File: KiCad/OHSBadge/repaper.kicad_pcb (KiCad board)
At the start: 2 copper layers, 101.6 x 78.7 mm, 76 parts, among them J4 ZIF-40-0.5, P1 PCB, P2 ISP, P3 FTDI, P4 C3SB, P6 3V3_SEL, Q1 AP2305, Q2 2N7002KW, Q3 BSS84W, Q4 2N7002KW, Q5 2N7002KW, Q6 2N7002KW, Q7 BSS84W, SW1 UP, SW2 SEL, SW3 DOWN, SW4 RST, U1 MCP9700AT-E/TT, U2 ATMEGA328-AU-ND, U3 MCP1700T-33, U4 TXS0108, X1 CRYSTAL_8MHz

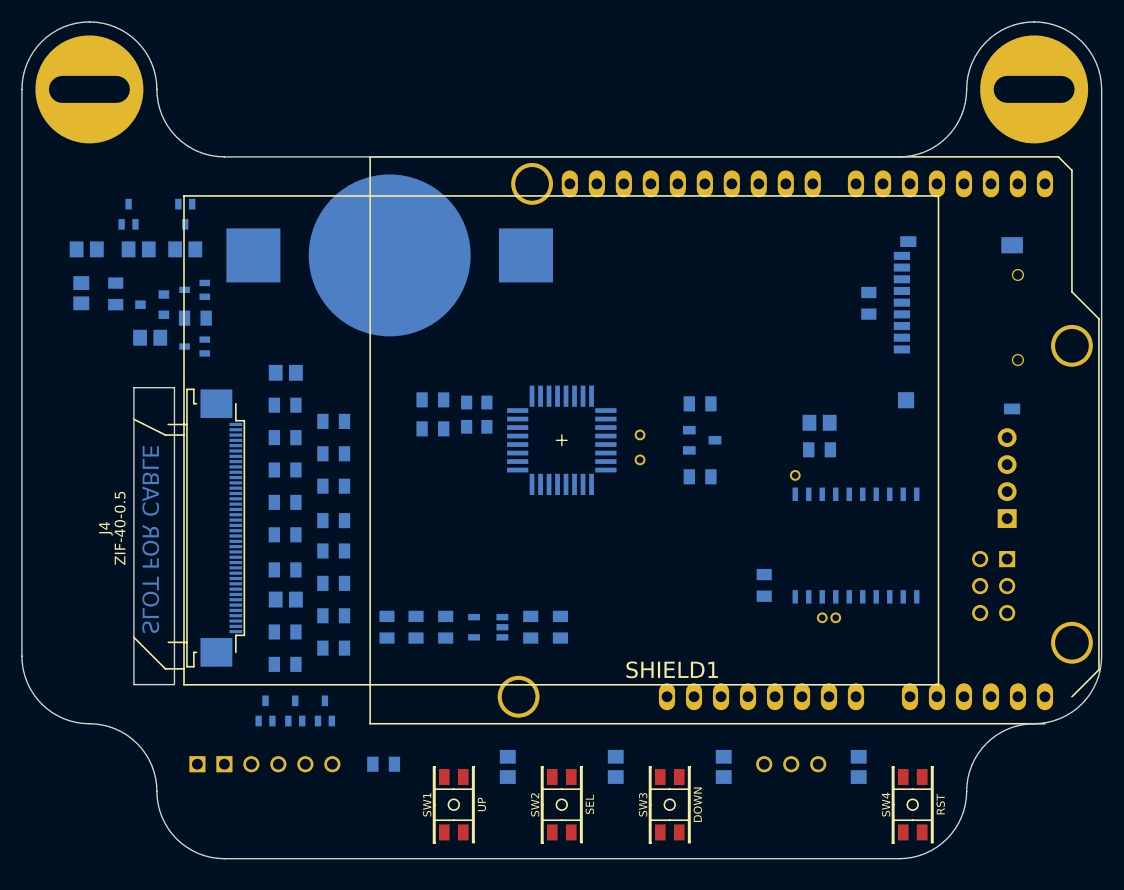
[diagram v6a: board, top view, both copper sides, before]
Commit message: OHSBadge - getting some basic track layout done
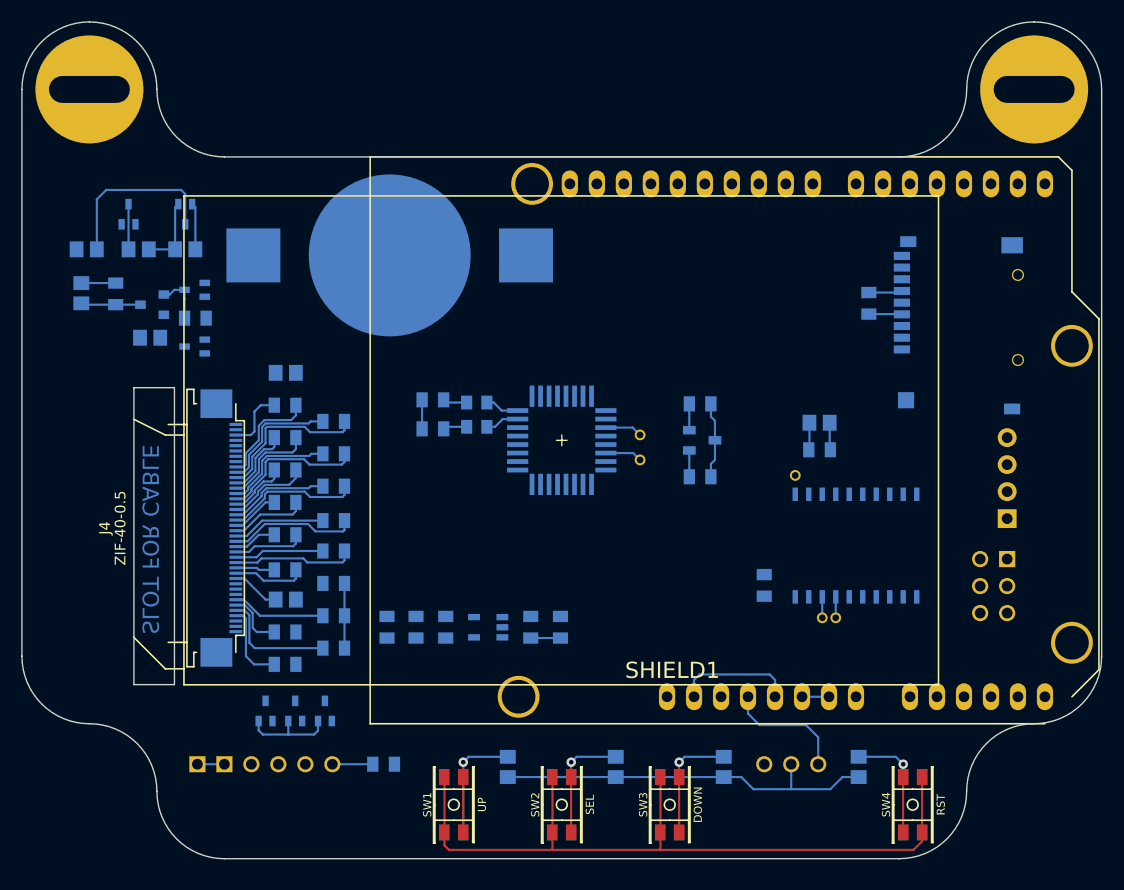
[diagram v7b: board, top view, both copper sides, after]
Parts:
- turned C15 to 180 degrees
- turned C17 to 180 degrees
- turned C19 to 180 degrees
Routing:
- net GND: track 0.00 -> 119.4 mm
- net /3V3: track 0.00 -> 44.5 mm
- net /BORDER: track 0.00 -> 16.4 mm
- net /C42M: track 0.00 -> 14.8 mm
- net /C31P: track 0.00 -> 13.7 mm
- net /C16P: track 0.00 -> 12.7 mm
- net /C14P: track 0.00 -> 12.1 mm
- net /VDL: track 0.00 -> 12.0 mm
- net /C42P: track 0.00 -> 11.7 mm
- net /VCC3V: track 0.00 -> 11.7 mm
- net /C12P: track 0.00 -> 11.5 mm
- net /VCC5V: track 0.00 -> 11.2 mm
- net /VDH: track 0.00 -> 11.2 mm
- net /UP: track 0.00 -> 11.0 mm, vias 0 -> 1
- net /SEL: track 0.00 -> 11.0 mm, vias 0 -> 1
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
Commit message: OHSBadge - track layout in progress
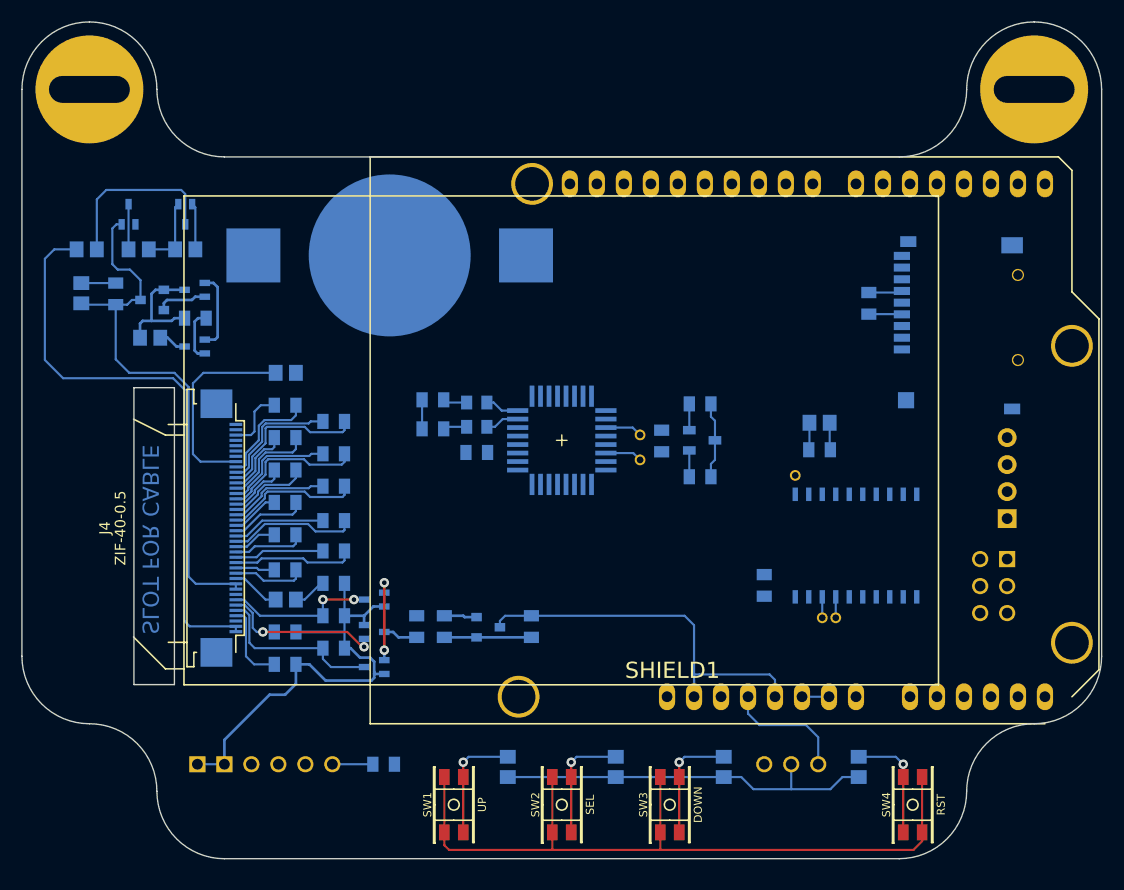
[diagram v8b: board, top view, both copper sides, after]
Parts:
- U3: footprint SOT23-5 -> SOT23
- moved C27 26.8 mm to (85.6, 75.0), turned to 270 degrees
- moved C29 17.2 mm to (68.2, 76.1), turned to 0 degrees
- moved Q4 11.5 mm to (58.5, 89.9), turned to 90 degrees
- moved Q5 11.0 mm to (58.5, 96.3), turned to 90 degrees
- moved D1 10.5 mm to (58.5, 93.0), turned to 270 degrees
- moved C26 2.79 mm to (62.5, 92.5)
- moved C30 2.73 mm to (73.3, 92.5)
- moved C28 2.67 mm to (65.2, 92.5)
- moved Q1 0.44 mm to (37.7, 61.7)
- turned U3 to 90 degrees
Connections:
- BT1 pad +: N-0000050 -> /Batt_3V
- C28 pad 1: N-0000050 -> /Batt_3V
- H1 pad 1: N-0000050 -> /Batt_3V
- P2 pad 1: /SPI_MISO -> /SPI_MISO_3V3
- P2 pad 2: /VCC5V -> /3V3
- P2 pad 3: /SPI_CLK -> /SPI_CLK_3V3
- P2 pad 4: /SPI_MOSI -> /SPI_MOSI_3V3
- P2 pad 5: /RST -> /RST_3V3
- P6 pad 3: N-0000050 -> /Batt_3V
- SHIELD1 pad 1: /TXD_3V3 -> /TXD
- SHIELD1 pad 11: /SPI_MOSI -> (no net)
- SHIELD1 pad 12: /SPI_MISO -> (no net)
- SHIELD1 pad 13: /SPI_CLK -> (no net)
- SHIELD1 pad RST: (no net) -> /RST
- U3 pad 2: /VCC5V -> /Batt_3V
- U3 pad 3: N-0000050 -> /VCC5V
- U4 pad 12: /RXD -> /TXD
- U4 pad 13: /TXD -> /RXD
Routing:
- net /VCOM: track 0.00 -> 57.7 mm
- net /VCC_T: track 5.62 -> 51.5 mm
- net GND: track 119.4 -> 157.3 mm
- net /VCC5V: track 11.2 -> 37.2 mm
- net N-0000039: track 0.00 -> 19.2 mm
- net /VGL: track 5.49 -> 17.4 mm, vias 0 -> 2
- net /DISCHARGE: track 0.00 -> 8.23 mm, vias 0 -> 2
- net /PANEL_ON: track 0.00 -> 7.38 mm
- net N-000001: track 4.80 -> 11.5 mm
- net /VGH: track 8.81 -> 14.2 mm, vias 0 -> 2
- net /VDH: track 11.2 -> 16.4 mm
- net /3V3: track 44.5 -> 49.2 mm
- net N-0000038: track 0.00 -> 3.26 mm
- net /Batt_3V: track 0.00 -> 3.08 mm
- net N-000002: track 0.00 -> 2.63 mm
